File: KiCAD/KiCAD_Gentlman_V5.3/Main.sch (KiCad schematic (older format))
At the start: 11 parts, among them CN1 SMW2.5MM-7P, U1 STM32G070RBT6, U2 W25Q32JVSS

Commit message: KSG : V5.3 회로도 초본 완성(검토 필요) 일부 부품 데이터시트 추가
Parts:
- added C10, C8, C9: CAP_105Z_6.3V_1608, symbol Custom:CAP_105Z_6.3V_1608
- added C11, C12: CAP_103K_25V_1608, symbol Custom:CAP_103K_25V_1608
- added C13, C14, C7: CAP_104Z_25V_1608, symbol Custom:CAP_104Z_25V_1608
- added C15, C16: CAP_220uF_6.3V_SC6.3X5.8, symbol Custom:CAP_220uF_6.3V_SC6.3X5.8
- added C6: 220uF_6.3V_SC6.3X5.8, symbol Custom:CAP_220uF_6.3V_SC6.3X5.8
- added CN2, CN3: 12505WR-02, symbol Custom:Conn_01x02
- added CN4: USB-TYPE-C-31-M-17, symbol Custom:USB-TYPE-C-31-M-17
- added D1, D2, D3, D4, D5, D6, D7: WR106SR-W, symbol Custom:WR106SR-W
- added K1_L, K1_R, K2_L, K2_R, K3_L, K3_R, K4_L, K4_R, K5_L, K5_R: SW_Push, symbol Custom:SW_Push
- added Q1, Q2, Q3, Q4, Q5, Q6: 2SA1981SY, Package_TO_SOT_SMD:TSOT-23, symbol Custom:2SA1981SY
- added R10, R9: R_NC, symbol Custom:R_NC
- added R11, R12, R13, R14, R23, R24: R_1KF, symbol Custom:R_1KF
- added R15, R16, R17, R18, R19: R_47RJ, symbol Custom:R_47RJ
- added R2, R3, R4, R5, R6, R7: R_390RJ, symbol Custom:R_390RJ
- added R20, R21, R22: R_10KJ, symbol Custom:R_10KJ
- added R25: R_22KJ, symbol Custom:R_22KJ
- added R26, R27: R_4.7KF, symbol Custom:R_4.7KF
- added R28: R_270RF, symbol Custom:R_270RF
- added R29: R_510RF, symbol Custom:R_510RF
- added RGB1, RGB2, RGB3, RGB4, RGB5: BL-HBHG8JE36K-TRB-T05, symbol Custom:BL-HBHG8JE36K-TRB-T05
- added TVS1: SMBJ15A, symbol Custom:SMBJ15A
- added U4: AP4890, symbol Custom:AP4890
- added U5: ULN2003D1013TR, digikey-footprints:SOIC-16_W3.90mm, symbol Custom:ULN2003D1013TR
- added U6: LMT117-ADJ, Package_TO_SOT_SMD:SOT-223-3_TabPin2, symbol Custom:LMT117-ADJ
- CN1: Field4 (none) -> DOWNLOAD
- gave numbers to parts that had none: 2
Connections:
- net labels added: +5V, CH1_P1_CTL1, CH1_P1_CTL2, CH1_P2_CTL1, CH1_P2_CTL2, CH2_P1_CTL1, CH2_P1_CTL2, CH2_P2_CTL1, CH2_P2_CTL2, CH3_P1_CTL1, CH3_P1_CTL2, CH3_P2_CTL1, CH3_P2_CTL2, CH3_P3_CTL1, CH3_P3_CTL2, CH3_P4_CTL1, CH3_P4_CTL2, CH4_P1_CTL1, CH4_P1_CTL2, CH4_P2_CTL1, CH4_P2_CTL2, CH4_P3_CTL1, CH4_P3_CTL2, CH4_P4_CTL1, CH4_P4_CTL2, CTL_CH1, CTL_CH2, CTL_CH3, CTL_CH4, H_CURR_CH, H_VOLT_CH1, H_VOLT_CH2, H_VOLT_CH3, H_VOLT_CH4, RGB_B6, RGB_COM6, RGB_G6, RGB_R6
- wire segments 44 -> 359
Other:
- moved on the sheet: R8, U3

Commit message: KSG : V5.3 회로도 완성, 심볼 정보 업데이트 완료(데이터시트 및 풋프린트 등), 기존 BOM과 일치 완료
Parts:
- C1, C13, C14, C2, C3, C4, C5, C7: footprint (none) -> Custom:C_0603_1608Metric; Comment (none) -> 104Z/25V; Description (none) -> CHIP CERAMIC CAP; MAKER (none) -> WALSIN, SAMSUNG; TYPE (none) -> 1608
- C10, C8, C9: footprint (none) -> Custom:C_0603_1608Metric; Comment (none) -> 105Z/6.3V; Description (none) -> CHIP CERAMIC CAP; MAKER (none) -> WALSIN, SAMSUNG; TYPE (none) -> 1608
- C11, C12: footprint (none) -> Custom:C_0603_1608Metric; Comment (none) -> 103K/25V; Description (none) -> CHIP CERAMIC CAP; MAKER (none) -> WALSIN, SAMSUNG; TYPE (none) -> 1608
- C15, C16: footprint (none) -> Custom:C_Elec_6.3x5.8; Comment (none) -> 220uF/6.3V; Description (none) -> SMD ELECT CAPACITOR; Field4 (none) -> 220uF/6.3V; MAKER (none) -> SAMYOUNG; TYPE (none) -> SC 6.3X5.8; ValueView 220uF/6.3V -> (none)
- C6: value 220uF_6.3V_SC6.3X5.8 -> CAP_220uF_6.3V_SC6.3X5.8; footprint (none) -> Custom:C_Elec_6.3x5.8; Comment (none) -> 220uF/6.3V; Description (none) -> SMD ELECT CAPACITOR; Field4 (none) -> 220uF/6.3V; MAKER (none) -> SAMYOUNG; TYPE (none) -> SC 6.3X5.8; ValueView 220uF/6.3V -> (none)
- CN1: footprint (none) -> Custom:SIP-7_P2.54mm; symbol Custom:Conn_01x07 -> Custom:SIP-7_P2.54mm; Comment (none) -> SMW2.5MM-7P; Description (none) -> PIN HEADER; MAKER (none) -> YEONHO ELECTRONICS; TYPE (none) -> DIP-8
- CN2, CN3: footprint (none) -> Custom:12505WR-02; symbol Custom:Conn_01x02 -> Custom:12505WR-02; Comment (none) -> 12505WR-02; Description (none) -> SMD WAFER; MAKER (none) -> YEONHO ELECTRONICS; TYPE (none) -> SMD-2
- CN4: footprint (none) -> Custom:TYPE-C-31-M-17-1; Comment (none) -> USB-TYPE-C-31-M-17; Description (none) -> SMD JACK USB C TYPE; MAKER (none) -> Korean-Hroparts-Elec; TYPE (none) -> SMD-6
- D1, D2, D3, D4, D5, D6, D7: footprint (none) -> Custom:LED_0603_1608Metric; Comment (none) -> WR106SR-W; Description (none) -> CHIP LED RED; MAKER (none) -> BRIGHT LED; TYPE (none) -> 1608
- K1_L1: renamed from K1_L; footprint (none) -> Custom:SW_Strom; Comment (none) -> SW_Push; Description (none) -> SWICH; TYPE (none) -> SW_Push
- K1_R1: renamed from K1_R; footprint (none) -> Custom:SW_Strom; Comment (none) -> SW_Push; Description (none) -> SWICH; TYPE (none) -> SW_Push
- K2_L1: renamed from K2_L; footprint (none) -> Custom:SW_Strom; Comment (none) -> SW_Push; Description (none) -> SWICH; TYPE (none) -> SW_Push
- K2_R1: renamed from K2_R; footprint (none) -> Custom:SW_Strom; Comment (none) -> SW_Push; Description (none) -> SWICH; TYPE (none) -> SW_Push
- K3_L1: renamed from K3_L; footprint (none) -> Custom:SW_Strom; Comment (none) -> SW_Push; Description (none) -> SWICH; TYPE (none) -> SW_Push
- K3_R1: renamed from K3_R; footprint (none) -> Custom:SW_Strom; Comment (none) -> SW_Push; Description (none) -> SWICH; TYPE (none) -> SW_Push
- K4_L1: renamed from K4_L; footprint (none) -> Custom:SW_Strom; Comment (none) -> SW_Push; Description (none) -> SWICH; TYPE (none) -> SW_Push
- K4_R1: renamed from K4_R; footprint (none) -> Custom:SW_Strom; Comment (none) -> SW_Push; Description (none) -> SWICH; TYPE (none) -> SW_Push
- K5_L1: renamed from K5_L; footprint (none) -> Custom:SW_Strom; Comment (none) -> SW_Push; Description (none) -> SWICH; TYPE (none) -> SW_Push
- K5_R1: renamed from K5_R; footprint (none) -> Custom:SW_Strom; Comment (none) -> SW_Push; Description (none) -> SWICH; TYPE (none) -> SW_Push
- Q1, Q2, Q3, Q4, Q5, Q6: footprint Package_TO_SOT_SMD:TSOT-23 -> Custom:SOT-23; Comment (none) -> 2SA1981SY; Description (none) -> CHIP TRANSISTOR; MAKER (none) -> AUK; TYPE (none) -> SOT-23
- R1, R20, R21, R22: footprint (none) -> Custom:R_0603_1608Metric; Comment (none) -> 10KJ; Description (none) -> CHIP RESISTOR; MAKER (none) -> WALSIN, SAMSUNG; TYPE (none) -> 1608
- R10, R8, R9: footprint (none) -> Custom:R_0603_1608Metric; Comment (none) -> NC; Description (none) -> CHIP RESISTOR; MAKER (none) -> WALSIN, SAMSUNG; TYPE (none) -> 1608
- R11, R12, R13, R14, R23, R24: footprint (none) -> Custom:R_0603_1608Metric; Comment (none) -> 1KF; Description (none) -> CHIP RESISTOR; MAKER (none) -> WALSIN, SAMSUNG; TYPE (none) -> 1608
- R15, R16, R17, R18, R19: footprint (none) -> Custom:R_0603_1608Metric; Comment (none) -> 47RJ; Description (none) -> CHIP RESISTOR; MAKER (none) -> WALSIN, SAMSUNG; TYPE (none) -> 1608
- R2, R3, R4, R5, R6, R7: footprint (none) -> Custom:R_0603_1608Metric; Comment (none) -> 390RJ; Description (none) -> CHIP RESISTOR; MAKER (none) -> WALSIN, SAMSUNG; TYPE (none) -> 1608
- R25: footprint (none) -> Custom:R_0603_1608Metric; Comment (none) -> 22KJ; Description (none) -> CHIP RESISTOR; MAKER (none) -> WALSIN, SAMSUNG; TYPE (none) -> 1608
- R26, R27: footprint (none) -> Custom:R_0603_1608Metric; Comment (none) -> 4.7KF; Description (none) -> CHIP RESISTOR; MAKER (none) -> WALSIN, SAMSUNG; TYPE (none) -> 1608
- R28: footprint (none) -> Custom:R_0603_1608Metric; Comment (none) -> 270RF; Description (none) -> CHIP RESISTOR; MAKER (none) -> WALSIN, SAMSUNG; TYPE (none) -> 1608
- R29: footprint (none) -> Custom:R_0603_1608Metric; Comment (none) -> 510RF; Description (none) -> CHIP RESISTOR; MAKER (none) -> WALSIN, SAMSUNG; TYPE (none) -> 1608
- RGB1, RGB2, RGB3, RGB4, RGB5: footprint (none) -> Custom:LED_RGB_0605; Comment (none) -> BL-HBHG8JE36K-TRB-T05; Description (none) -> CHIP LED RGB; MAKER (none) -> BRIGHT LED; TYPE (none) -> 1615
- TVS1: footprint (none) -> Custom:D_SMB; Comment (none) -> SMBJ15A; Description (none) -> SMD DIODE TVS; MAKER (none) -> SAMYANG ELECTRONICS; TYPE (none) -> SMB
- U1: footprint QFP50P1200X1200X160-64N -> Custom:LQFP-64_10x10mm_P0.5mm; symbol STM32G070RBT6:STM32G070RBT6 -> Custom:STM32G070RBT6; A1_MIN 0.15 -> (none); A_MAX 1.6 -> (none); B_MAX 0.27 -> (none); B_MIN 0.17 -> (none); B_NOM 0.22 -> (none); Comment (none) -> STM32G070RBT6; D1_MAX 10.0 -> (none); D1_MIN 10.0 -> (none); D1_NOM 10.0 -> (none); D2_NOM 0.0 -> (none); D_MAX 12.0 -> (none); D_MIN 12.0 -> (none); D_NOM 12.0 -> (none); Description (none) -> SMD MCU; E1_MAX 10.0 -> (none); E1_MIN 10.0 -> (none); E1_NOM 10.0 -> (none); E2_NOM 0.0 -> (none); ENOM 0.5 -> (none); E_MAX 12.0 -> (none); E_MIN 12.0 -> (none); E_NOM 12.0 -> (none); L_MAX 0.75 -> (none); L_MIN 0.45 -> (none); L_NOM 0.6 -> (none); MAKER (none) -> STMicroelectronics; MANUFACTURER ST -> (none); MAXIMUM_PACKAGE_HEIGHT 1.6mm -> (none); PARTREV 1 -> (none); PIN_COUNT_D 16.0 -> (none); PIN_COUNT_E 16.0 -> (none); STANDARD IPC 7351B -> (none); TYPE (none) -> LQFP64
- U2: footprint Package_SO:SOIC-8_5.23x5.23mm_P1.27mm -> Custom:SOIC-8_5.23x5.23mm_P1.27mm; Comment (none) -> W25Q32JVSSIQ; Description (none) -> SMD SERIAL FLASH; MAKER (none) -> WINBOND; TYPE (none) -> SOIC-8(208mil)
- U3: footprint (none) -> Custom:SOP-8_3.76x4.96mm_P1.27mm; Comment (none) -> VLN1MM04S8X; Description (none) -> SMD VOICE; MAKER (none) -> SYNOOS; TYPE (none) -> SOP-8
- U4: footprint (none) -> Custom:SOP-8_3.76x4.96mm_P1.27mm; Comment (none) -> AP4890; Description (none) -> SMD AMPLIFIER 1W; MAKER (none) -> APLUS; TYPE (none) -> SOP8
- U5: footprint digikey-footprints:SOIC-16_W3.90mm -> Custom:SOIC-16_3.9x9.9mm_P1.27mm; Category Discrete Semiconductor Products -> (none); Comment (none) -> ULN2003D1013TR; DK_Datasheet_Link http://www.st.com/content/ccc/resource/technical/document/d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 -> (none); DK_Detail_Page /product-detail/en/stmicroelectronics/ULN2003D1013TR/497-23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 -> (none); Description IC PWR RELAY 7NPN 1:1 16SO -> SMD BUFFER; Digi-Key_PN 497-2345-1-ND -> (none); Family Transistors - Bipolar (BJT) - Arrays -> (none); MAKER (none) -> STMicroelectronics; MPN ULN2003D1013TR -> (none); Manufacturer STMicroelectronics -> (none); Status Active -> (none); TYPE (none) -> SOP-16
- U6: footprint Package_TO_SOT_SMD:SOT-223-3_TabPin2 -> Custom:SOT-223-3_TabPin2; Comment (none) -> LMT117-ADJ; Description (none) -> SMD REGULATOR; MAKER (none) -> TGS; TYPE (none) -> SOT-223

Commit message: KSG : 블루투스 회로도 작성 완료 (풋프린트 및 데이터시트 업데이트 완료)
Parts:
- CN1: value SMW2.5MM-7P -> PinHeader2.54mm_7; footprint Custom:SIP-7_P2.54mm -> Custom:PinHeader_1x07_P2.54mm_Vertical; symbol Custom:SIP-7_P2.54mm -> Custom:PinHeader2.54mm_7; Comment SMW2.5MM-7P -> PinHeader2.54mm-7P; TYPE DIP-8 -> DIP-7
- renumbered CN4 to J4
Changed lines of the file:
@@
 $Descr A3 16535 11693
 encoding utf-8
-Sheet 2 3
+Sheet 2 4
 Title "GentlemanV5.3"
 Date "2021-10-19"
@@
 Wire Wire Line
 	5950 1400 6100 1400
-$Comp
-L Custom:SIP-7_P2.54mm CN1
-U 1 1 61770F03
-P 1850 2900
-AR Path="/61770F03" Ref="CN1"  Part="1"
-AR Path="/616E62D0/61770F03" Ref="CN1"  Part="1"
-F 0 "CN1" H 1850 3300 50  0000 C CNN
-F 1 "SMW2.5MM-7P" H 1850 2500 50  0000 C CNN
-F 2 "Custom:SIP-7_P2.54mm" H 1850 2900 50  0001 C CNN
-F 3 ".\\Dataseets\\12505-NN.pdf" H 1850 2900 50  0001 C CNN
-F 4 "DOWNLOAD" V 1950 2900 50  0000 C CNN "Field4"
-F 5 "SMW2.5MM-7P" H 1850 2900 50  0001 C CNN "Comment"
-F 6 "PIN HEADER" H 1850 2900 50  0001 C CNN "Description"
-F 7 "YEONHO ELECTRONICS" H 1850 2900 50  0001 C CNN "MAKER"
-F 8 "DIP-8" H 1850 2900 50  0001 C CNN "TYPE"
-	1    1850 2900
-	-1   0    0    -1
-$EndComp
 Wire Wire Line
 	2050 2700 2600 2700
@@
 P 950 4900
 AR Path="/619AE106" Ref="CN2"  Part="1"
-AR Path="/616E62D0/619AE106" Ref="CN2"  Part="1"
-F 0 "CN2" H 950 5000 50  0000 C CNN
+AR Path="/616E62D0/619AE106" Ref="J2"  Part="1"
+F 0 "J2" H 950 5000 50  0000 C CNN
 F 1 "12505WR-02" H 950 4700 50  0000 C CNN
 F 2 "Custom:12505WR-02" H 950 4900 50  0001 C CNN
@@
 P 950 5900
 AR Path="/619DDEDC" Ref="CN3"  Part="1"
-AR Path="/616E62D0/619DDEDC" Ref="CN3"  Part="1"
-F 0 "CN3" H 950 6000 50  0000 C CNN
+AR Path="/616E62D0/619DDEDC" Ref="J3"  Part="1"
+F 0 "J3" H 950 6000 50  0000 C CNN
 F 1 "12505WR-02" H 950 5700 50  0000 C CNN
 F 2 "Custom:12505WR-02" H 950 5900 50  0001 C CNN
@@
 $EndComp
 $Comp
-L Custom:USB-TYPE-C-31-M-17 CN4
+L Custom:USB-TYPE-C-31-M-17 J4
 U 1 1 61FD82ED
 P 9750 8200
-F 0 "CN4" H 9400 8600 50  0000 C CNN
+F 0 "J4" H 9400 8600 50  0000 C CNN
 F 1 "USB-TYPE-C-31-M-17" H 9750 7800 50  0000 C CNN
 F 2 "Custom:TYPE-C-31-M-17-1" H 9900 8200 50  0001 C CNN
@@
 	1    0    0    -1
 $EndComp
+$Comp
+L Custom:PinHeader2.54mm_7 CN1
+U 1 1 61770F03
+P 1850 2900
+AR Path="/61770F03" Ref="CN1"  Part="1"
+AR Path="/616E62D0/61770F03" Ref="J1"  Part="1"
+F 0 "J1" H 1850 3300 50  0000 C CNN
+F 1 "PinHeader2.54mm_7" H 1850 2500 50  0000 C CNN
+F 2 "Custom:PinHeader_1x07_P2.54mm_Vertical" H 1850 2900 50  0001 C CNN
+F 3 "~" H 1850 2900 50  0001 C CNN
+F 4 "DOWNLOAD" V 1950 2900 50  0000 C CNN "Field4"
+F 5 "PinHeader2.54mm-7P" H 1850 2900 50  0001 C CNN "Comment"
+F 6 "PIN HEADER" H 1850 2900 50  0001 C CNN "Description"
+F 7 "YEONHO ELECTRONICS" H 1850 2900 50  0001 C CNN "MAKER"
+F 8 "DIP-7" H 1850 2900 50  0001 C CNN "TYPE"
+	1    1850 2900
+	-1   0    0    -1
+$EndComp
 $EndSCHEMATC

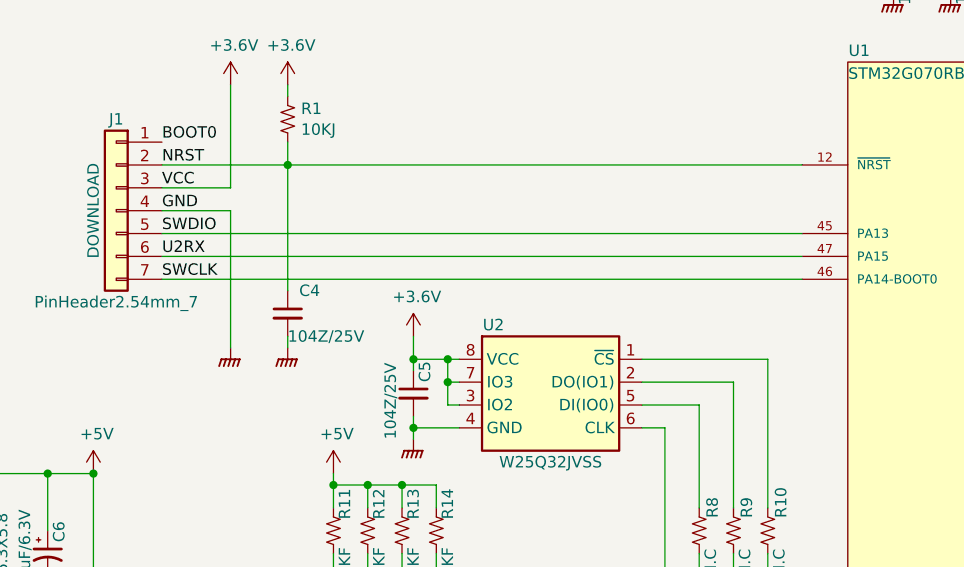
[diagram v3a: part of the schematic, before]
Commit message: KSG : 반이중통신용 회로도 구성 완료
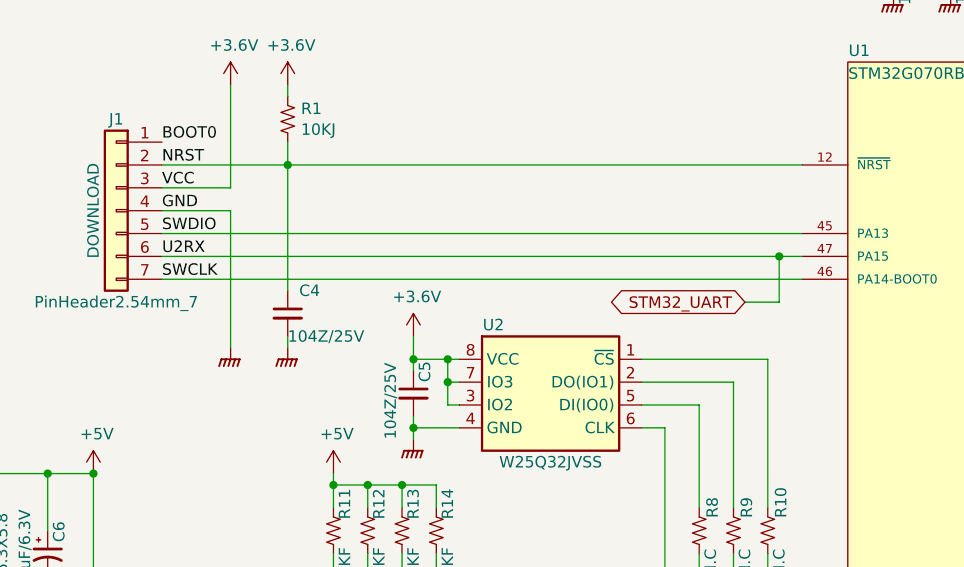
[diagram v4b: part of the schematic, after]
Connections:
- net U2RX renamed STM32_UART
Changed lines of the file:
@@
 	2050 3000 4850 3000
 Wire Wire Line
-	2050 3100 4850 3100
+	2050 3100 4750 3100
 Wire Wire Line
 	2050 3200 4850 3200
@@
 	-1   0    0    -1
 $EndComp
+Text GLabel 4600 3300 0    50   BiDi ~ 0
+STM32_UART
+Wire Wire Line
+	4600 3300 4750 3300
+Wire Wire Line
+	4750 3300 4750 3100
+Connection ~ 4750 3100
+Wire Wire Line
+	4750 3100 4850 3100
 $EndSCHEMATC

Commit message: KSG : V5.3B용으로 회로도 수정 및 PCB 아트웤 완료.(샘플PCB주문됨)
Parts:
- removed C10, C8, C9: CAP_105Z_6.3V_1608, Custom:C_0603_1608Metric, symbol Custom:CAP_105Z_6.3V_1608
- removed C11, C12: CAP_103K_25V_1608, Custom:C_0603_1608Metric, symbol Custom:CAP_103K_25V_1608
- removed C5: CAP_104Z_25V_1608, Custom:C_0603_1608Metric, symbol Custom:CAP_104Z_25V_1608
- removed CN3: 12505WR-02, Custom:12505WR-02, symbol Custom:12505WR-02
- removed K1_L1, K1_R1, K2_L1, K2_R1, K3_L1, K3_R1, K4_L1, K4_R1, K5_L1, K5_R1: SW_Push, Custom:SW_Strom, symbol Custom:SW_Push
- removed R10, R8, R9: R_NC, Custom:R_0603_1608Metric, symbol Custom:R_NC
- removed R20, R21, R22: R_10KJ, Custom:R_0603_1608Metric, symbol Custom:R_10KJ
- removed R23, R24: R_1KF, Custom:R_0603_1608Metric, symbol Custom:R_1KF
- removed R25: R_22KJ, Custom:R_0603_1608Metric, symbol Custom:R_22KJ
- removed U2: W25Q32JVSS, Custom:SOIC-8_5.23x5.23mm_P1.27mm, symbol Custom:W25Q32JVSS
- removed U4: AP4890, Custom:SOP-8_3.76x4.96mm_P1.27mm, symbol Custom:AP4890
- added J8: PinHeader2.54mm_2, Custom:PinHeader_1x02_P2.54mm_Vertical, symbol Custom:PinHeader2.54mm_2
- added SW1, SW2, SW3, SW4, SW5: SW_Tact_1105, Custom:SW_PUSH_6mm_H5mm, symbol Custom:SW_Tact_1105
- C1, C13, C14, C2, C3, C4, C7: Comment 104Z/25V -> (none); Description CHIP CERAMIC CAP -> (none); Field4 104Z/25V -> (none); MAKER WALSIN, SAMSUNG -> (none); Maker (none) -> WALSIN, SAMSUNG; PartName (none) -> 104Z/25V; Replacement (none) -> CL10B104KA8NNNC; Shop (none) -> https://www.eleparts.co.kr/goods/view?no=8010066; TYPE 1608 -> (none); Type (none) -> CHIP CERAMIC CAP
- C15, C16, C6: Comment 220uF/6.3V -> (none); Description SMD ELECT CAPACITOR -> (none); Field4 220uF/6.3V -> (none); Field5 SC 6.3X5.8 -> (none); MAKER SAMYOUNG -> (none); Maker (none) -> SAMYOUNG; PartName (none) -> 220uF/6.3V; Shop (none) -> https://www.eleparts.co.kr/goods/view?no=3369557; TYPE SC 6.3X5.8 -> (none); Type (none) -> SMD ELECT CAPACITOR
- CN1: Comment PinHeader2.54mm-7P -> (none); Description PIN HEADER -> (none); Field4 DOWNLOAD -> (none); MAKER YEONHO ELECTRONICS -> (none); PartName (none) -> PinHeader2.54mm-7P; TYPE DIP-7 -> (none); Type (none) -> PIN HEADER
- CN2: Comment 12505WR-02 -> (none); Description SMD WAFER -> (none); Field4 SPEAK1 -> (none); MAKER YEONHO ELECTRONICS -> (none); Maker (none) -> YEONHO ELECTRONICS; PartName (none) -> 12505WR-02; Shop (none) -> https://www.devicemart.co.kr/goods/view?no=1381566; TYPE SMD-2 -> (none); Type (none) -> SMD WAFER
- D1, D2, D3, D4, D5, D6, D7: Comment WR106SR-W -> (none); Description CHIP LED RED -> (none); MAKER BRIGHT LED -> (none); Maker (none) -> BRIGHT LED; PartName (none) -> WR106SR-W; Shop (none) -> https://www.eleparts.co.kr/goods/view?no=8104608; TYPE 1608 -> (none); Type (none) -> CHIP LED RED
- J4: Comment USB-TYPE-C-31-M-17 -> (none); Description SMD JACK USB C TYPE -> (none); MAKER Korean-Hroparts-Elec -> (none); Maker (none) -> Korean-Hroparts-Elec; PartName (none) -> USB-TYPE-C-31-M-17; TYPE SMD-6 -> (none); Type (none) -> SMD JACK USB C TYPE
- Q1, Q2, Q3, Q4, Q5, Q6: Comment 2SA1981SY -> (none); Description CHIP TRANSISTOR -> (none); MAKER AUK -> (none); Maker (none) -> AUK; PartName (none) -> 2SA1981SY; Replacement (none) -> MMBT200; Shop (none) -> https://www.eleparts.co.kr/goods/view?no=7467326; TYPE SOT-23 -> (none); Type (none) -> CHIP TRANSISTOR
- R1: Comment 10KJ -> (none); Description CHIP RESISTOR -> (none); Field4 10KJ -> (none); MAKER WALSIN, SAMSUNG -> (none); Maker (none) -> WALSIN, SAMSUNG; PartName (none) -> 10KJ; TYPE 1608 -> (none); Type (none) -> CHIP RESISTOR
- R11, R12, R13, R14: Comment 1KF -> (none); Description CHIP RESISTOR -> (none); Field4 1KF -> (none); MAKER WALSIN, SAMSUNG -> (none); Maker (none) -> WALSIN, SAMSUNG; PartName (none) -> 1KF; TYPE 1608 -> (none); Type (none) -> CHIP RESISTOR
- R15, R16, R17, R18, R19: Comment 47RJ -> (none); Description CHIP RESISTOR -> (none); Field4 47RJ -> (none); MAKER WALSIN, SAMSUNG -> (none); Maker (none) -> WALSIN, SAMSUNG; PartName (none) -> 47RJ; TYPE 1608 -> (none); Type (none) -> CHIP RESISTOR
- R2, R3, R4, R5, R6, R7: Comment 390RJ -> (none); Description CHIP RESISTOR -> (none); Field4 390RJ -> (none); MAKER WALSIN, SAMSUNG -> (none); Maker (none) -> WALSIN, SAMSUNG; PartName (none) -> 390RJ; TYPE 1608 -> (none); Type (none) -> CHIP RESISTOR
- R26, R27: Comment 4.7KF -> (none); Description CHIP RESISTOR -> (none); Field4 4.7KF -> (none); MAKER WALSIN, SAMSUNG -> (none); Maker (none) -> WALSIN, SAMSUNG; PartName (none) -> 4.7KF; TYPE 1608 -> (none); Type (none) -> CHIP RESISTOR
- R28: Comment 270RF -> (none); Description CHIP RESISTOR -> (none); Field4 270RF -> (none); MAKER WALSIN, SAMSUNG -> (none); Maker (none) -> WALSIN, SAMSUNG; PartName (none) -> 270RF; TYPE 1608 -> (none); Type (none) -> CHIP RESISTOR
- R29: Comment 510RF -> (none); Description CHIP RESISTOR -> (none); Field4 510RF -> (none); MAKER WALSIN, SAMSUNG -> (none); Maker (none) -> WALSIN, SAMSUNG; PartName (none) -> 510RF; TYPE 1608 -> (none); Type (none) -> CHIP RESISTOR
- RGB1, RGB2, RGB3, RGB4, RGB5: value BL-HBHG8JE36K-TRB-T05 -> 1615RGBC; symbol Custom:BL-HBHG8JE36K-TRB-T05 -> Custom:1615RGBC; Comment BL-HBHG8JE36K-TRB-T05 -> (none); Description CHIP LED RGB -> (none); MAKER BRIGHT LED -> (none); Maker (none) -> ZHUOYUEWEI; PartName (none) -> 1615RGBC; Shop (none) -> https://www.ic114.com/WebSite/SITE/sc/00V0.aspx?ID_P=P00853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; TYPE 1615 -> (none); Type (none) -> CHIP LED RGB
- TVS1: Comment SMBJ15A -> (none); Description SMD DIODE TVS -> (none); MAKER SAMYANG ELECTRONICS -> (none); Maker (none) -> SAMYANG ELECTRONICS; PartName (none) -> SMBJ15A; Shop (none) -> https://www.eleparts.co.kr/goods/view?no=6542453; TYPE SMB -> (none); Type (none) -> SMD DIODE TVS
- U1: Comment STM32G070RBT6 -> (none); Description SMD MCU -> (none); MAKER STMicroelectronics -> (none); Maker (none) -> STMicroelectronics; PartName (none) -> STM32G070RBT6; Shop (none) -> https://unit808.com/shop/goods_view.php?id=2967818949&brand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; TYPE LQFP64 -> (none); Type (none) -> SMD MCU
- U3: Comment VLN1MM04S8X -> (none); Description SMD VOICE -> (none); MAKER SYNOOS -> (none); Maker (none) -> SYNOOS; PartName (none) -> VLN1MM04S8X; TYPE SOP-8 -> (none); Type (none) -> SMD VOICE
- U5: Comment ULN2003D1013TR -> (none); Description SMD BUFFER -> (none); MAKER STMicroelectronics -> (none); Maker (none) -> STMicroelectronics; PartName (none) -> ULN2003D1013TR; Shop (none) -> https://www.eleparts.co.kr/goods/view?no=7572406; TYPE SOP-16 -> (none); Type (none) -> SMD BUFFER
- U6: Comment LMT117-ADJ -> (none); Description SMD REGULATOR -> (none); MAKER TGS -> (none); Maker (none) -> TGS; PartName (none) -> LMT117-ADJ; Replacement (none) -> LM1117S-ADJ; Shop (none) -> https://www.eleparts.co.kr/goods/view?no=6559295; TYPE SOT-223 -> (none); Type (none) -> SMD REGULATOR
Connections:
- net BOOT0 is gone; now on net +5V: CN1.1 (Pin_1)
- net +5V: now also TVS1.1 (A1); no longer TVS1.2 (A2)
- net GNDPWR: now also TVS1.2 (A2), SW1.2, SW2.2, SW3.2, SW4.2, SW5.2; no longer TVS1.1 (A1)
- net RGB_B6: now also RGB1.3 (BK), RGB2.3 (BK), RGB3.3 (BK), RGB4.3 (BK), RGB5.3 (BK); no longer RGB1.4 (BK), RGB2.4 (BK), RGB3.4 (BK), RGB4.4 (BK), RGB5.4 (BK)
- net RGB_G6: now also RGB1.2 (GK), RGB2.2 (GK), RGB3.2 (GK), RGB4.2 (GK), RGB5.2 (GK); no longer RGB1.3 (GK), RGB2.3 (GK), RGB3.3 (GK), RGB4.3 (GK), RGB5.3 (GK)
- net RGB_R6: now also RGB1.1 (RK), RGB2.1 (RK), RGB3.1 (RK), RGB4.1 (RK), RGB5.1 (RK); no longer RGB1.2 (RK), RGB2.2 (RK), RGB3.2 (RK), RGB4.2 (RK), RGB5.2 (RK)
- net at U1.10 (PF0-OSC_IN): now also SW5.1
- net at U1.17 (PA0): now also SW1.1
- net at U1.18 (PA1): now also SW2.1
- net at U1.22 (PA5): now also SW3.1
- net at U1.44 (PA12): now also SW4.1
- net at CN2.2 (Pin_2), U3.2 (PP2): now also J8.2 (Pin_2)
- net at CN2.1 (Pin_1), U3.7 (PP1): now also J8.1 (Pin_1)
- net at D1.2 (A), D7.2 (A), Q1.3 (C): now also RGB1.4 (A); no longer RGB1.1 (A)
- net at D2.2 (A), Q2.3 (C): now also RGB2.4 (A); no longer RGB2.1 (A)
- net at D3.2 (A), Q3.3 (C): now also RGB3.4 (A); no longer RGB3.1 (A)
- net at D4.2 (A), Q4.3 (C): now also RGB4.4 (A); no longer RGB4.1 (A)
- net at D5.2 (A), Q5.3 (C): now also RGB5.4 (A); no longer RGB5.1 (A)
- net STM32_UART renamed UART
- no-connect marks 0 -> 9
